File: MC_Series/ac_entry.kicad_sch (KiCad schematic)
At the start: 16 parts, among them U4 R-78E3.3-1.0

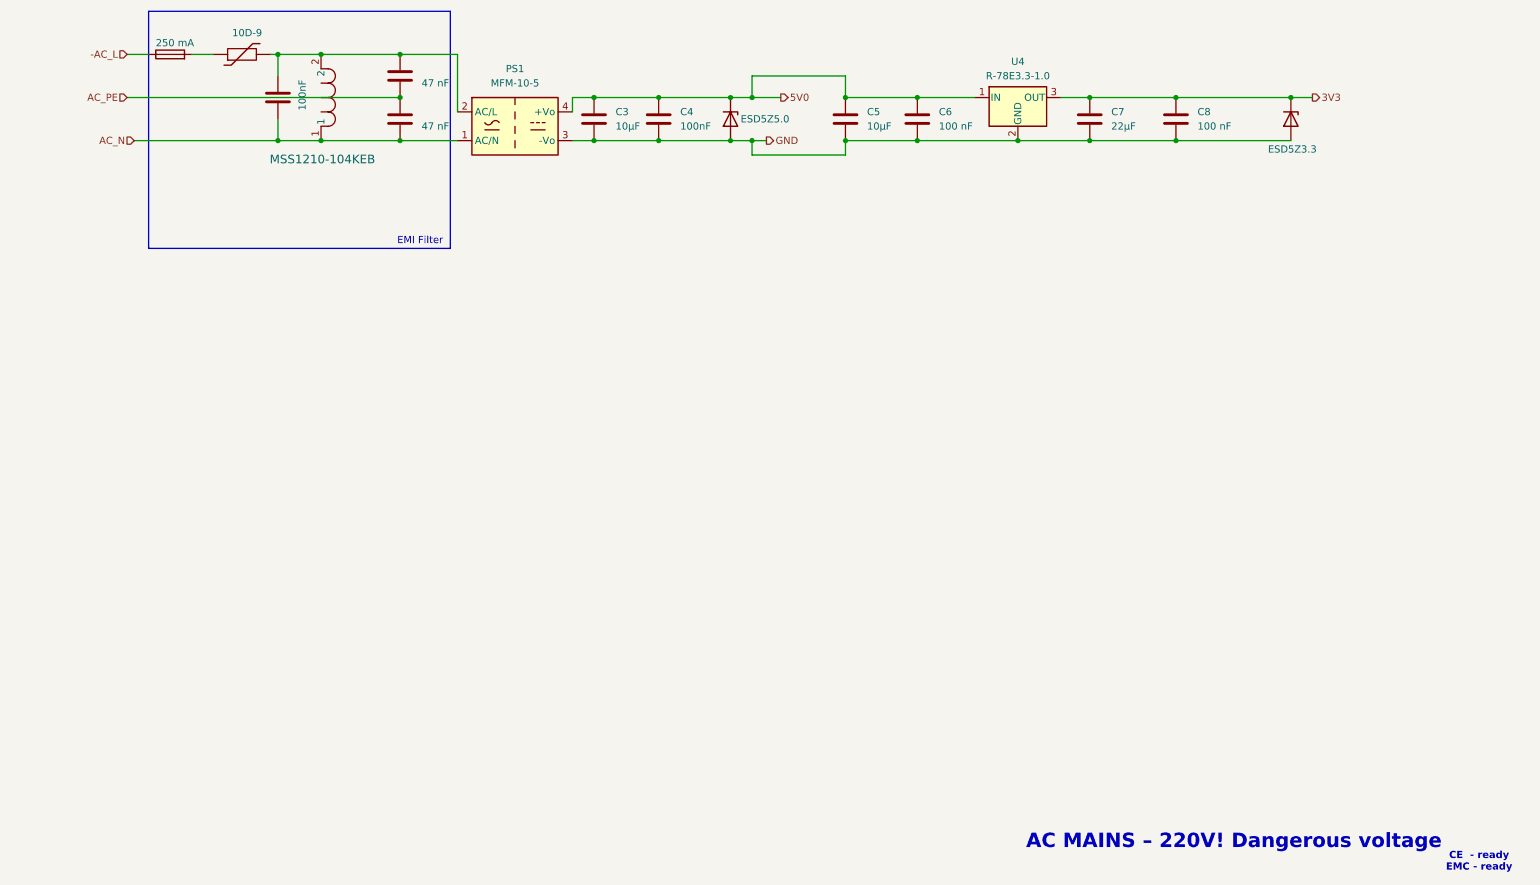
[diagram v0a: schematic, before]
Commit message: Proper namings in AC_ENTRY and CHANNEL + passives on root
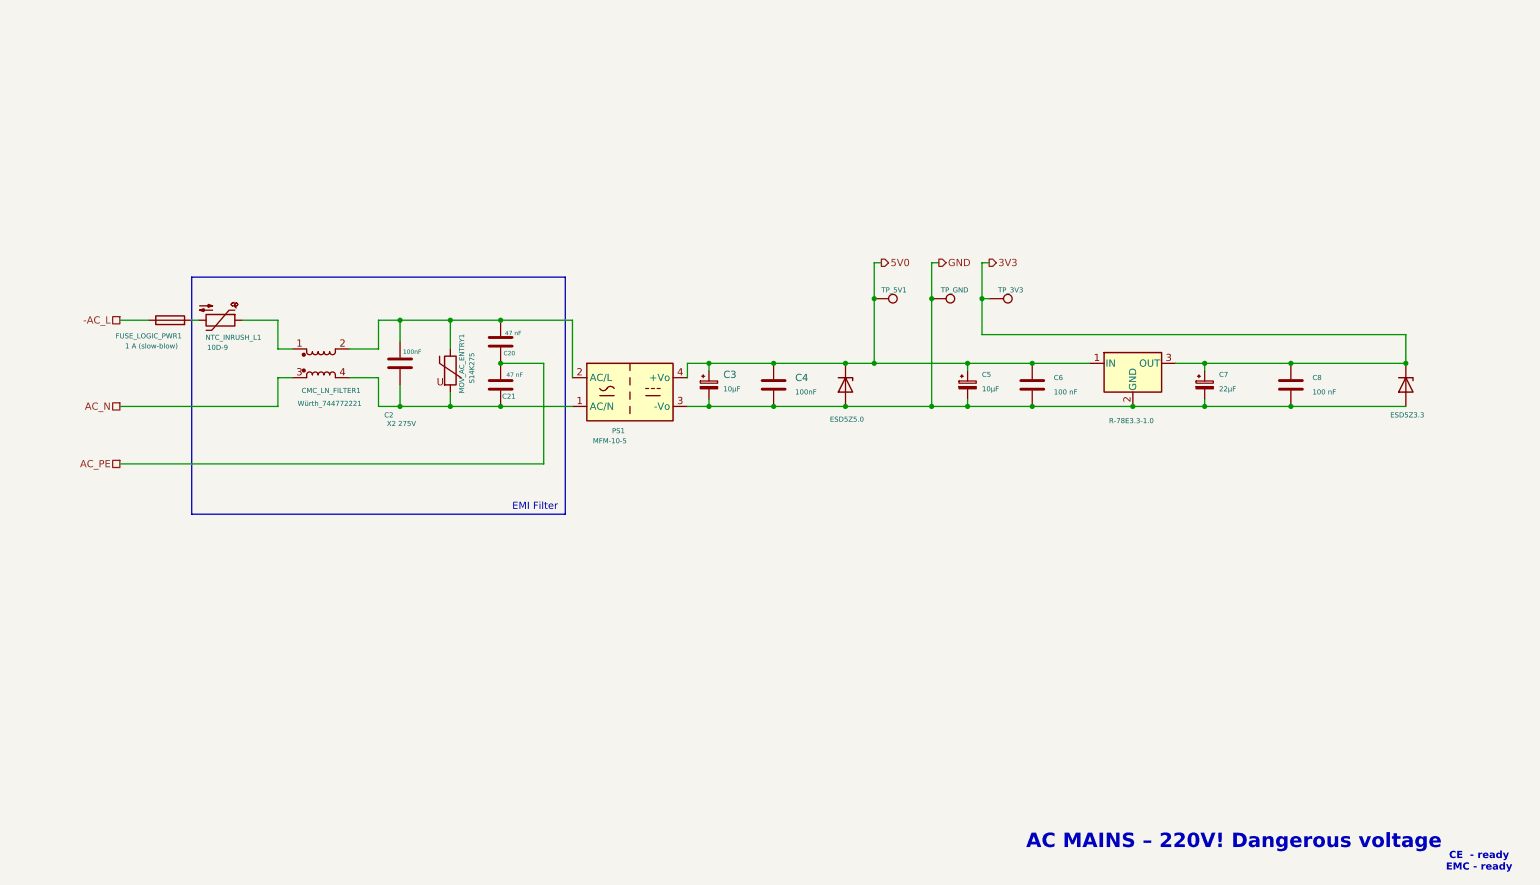
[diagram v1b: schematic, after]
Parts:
- removed C5: 10µF, symbol Device:C
- removed L2: MSS1210-104KEB, IND_MSS1210_COC, symbol nelees:MSS1210-104KEB
- removed TH1: 10D-9, symbol Device:Thermistor
- added C5: 10µF, symbol Device:C_Polarized_Small
- added CMC_LN_FILTER1: Würth_744772221, Inductor_SMD:L_Wuerth_WE-DD-Typ-L-Typ-XL-Typ-XXL, symbol Device:L_Coupled
- added MOV_AC_ENTRY1: S14K275, symbol Device:Varistor
- added NTC_INRUSH_L1: 10D-9, symbol Device:Thermistor_NTC
- added TP1: TP_GND, TestPoint:TestPoint_Pad_1.0x1.0mm, symbol Connector:TestPoint
- added TP2: TP_3V3, TestPoint:TestPoint_Pad_1.0x1.0mm, symbol Connector:TestPoint
- added TP_5V1: TP_5V0, TestPoint:TestPoint_Pad_1.0x1.0mm, symbol Connector:TestPoint
- C3, C7: symbol Device:C -> Device:C_Polarized_Small
- FUSE_LOGIC_PWR1: renamed from F1; value 250 mA -> 1 A (slow-blow)
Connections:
- net 3V3: now also TP2.1
- net 5V0: now also C5.1, TP_5V1.1
- net AC_N: now also CMC_LN_FILTER1.3; no longer C2.2, C21.2, PS1.1 (AC/N)
- net GND: now also C5.2, TP1.1
- net at FUSE_LOGIC_PWR1.2: now also NTC_INRUSH_L1.2
- net at C2.1, C20.1, PS1.2 (AC/L): now also CMC_LN_FILTER1.2, MOV_AC_ENTRY1.1
- new net: CMC_LN_FILTER1.1, NTC_INRUSH_L1.1
- new net: C2.2, C21.2, CMC_LN_FILTER1.4, MOV_AC_ENTRY1.2, PS1.1 (AC/N)
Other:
- moved on the sheet: C4, C6, C8, PS1

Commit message: Updated MC_Series template
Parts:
- removed NTC_INRUSH_L1: 10D-9, symbol Device:Thermistor_NTC
- added C_3V3_ESR1: 220µF/10V, symbol Device:C_Polarized_Small
- added MAIN_AC_INPUT1: Screw_Terminal_01x03, symbol Connector:Screw_Terminal_01x03
- added PTC_INRUSH_PROTECT1: MF-RX185/240, symbol Device:Thermistor_PTC
- D_ESD_5V0_OUT1: renamed from D14; value ESD5Z5.0 -> D_ESD_5V0_OUT
- renumbered C20 to CY2_L_PE1, C21 to CY2_N_PE1, C5 to C_3V3IN_BULK1, C6 to C_3V3IN_HF1, C7 to C_3V3_BULK1, C8 to C_3V3_HF1, C3 to C_5V_BULK1, C4 to C_5V_HF1, C2 to C_DIFF_EMI_FILTER1, D13 to D_ESD_3V3_OUT1, FUSE_LOGIC_PWR1 to F_LOGIC_MAIN1, U4 to REG_5TO_3V1, PS1 to REG_AC5V1
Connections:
- net 3V3: now also C_3V3_ESR1.1
- net AC_N: now also MOV_AC_ENTRY1.2, MAIN_AC_INPUT1.2 (Pin_2)
- net AC_PE: now also MAIN_AC_INPUT1.1 (Pin_1)
- net GND: now also C_3V3_ESR1.2
- net ­AC_L: now also MAIN_AC_INPUT1.3 (Pin_3)
- net at F_LOGIC_MAIN1.2: now also PTC_INRUSH_PROTECT1.2
- net at CMC_LN_FILTER1.1: now also MOV_AC_ENTRY1.1, PTC_INRUSH_PROTECT1.1
- net at CMC_LN_FILTER1.2, CY2_L_PE1.1, C_DIFF_EMI_FILTER1.1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: no longer MOV_AC_ENTRY1.1
- net at CMC_LN_FILTER1.4, CY2_N_PE1.2, C_DIFF_EMI_FILTER1.2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: no longer MOV_AC_ENTRY1.2
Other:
- moved on the sheet: CMC_LN_FILTER1, CY2_L_PE1, CY2_N_PE1, C_3V3IN_BULK1, C_3V3IN_HF1, C_3V3_BULK1, C_3V3_HF1, C_5V_BULK1, C_5V_HF1, C_DIFF_EMI_FILTER1, F_LOGIC_MAIN1, MOV_AC_ENTRY1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
